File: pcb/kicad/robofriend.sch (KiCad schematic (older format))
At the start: 124 parts, among them J1 UART, J10 12V-Buck, J11 12V-Buck-Boost, J12 5VIN, J13 5VOUT, J14 5VOUT, J15 US2, J16 US3, J17 USB_A_4_PIN, J18 12V-Reg, J19 MON/AMP, J2 VBAT, J20 US4, J21 MRi, J22 SPI, J23 MRi, J24 3V3OUT, J25 3V3OUT, J26 M1, J27 M2, J28 IR1, J29 ADC1, J3 PWR, J30 IR2, J31 ADC2, J32 IR3, J33 GS2, J4 GS2, J5 I2C, J6 I2C, J7 I2C, J8 I2C, J9 US1, K1 Schrak-RT334012, Q1 NMOS, Q2 NPN, Q3 PMOS, U1 74LVC1T45, U10 TL331, U2 Teensy++2.0, U3 TL331, U4 74LVC1T45, U5 PCA9517, U6 MCP6001, U7 LM3940-3.3, U8 LM4040, U9 INA193

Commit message: added new usb connector footprint to layout, minor adaptations, generated gerber and drill files, new plot available
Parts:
- J17: footprint USB_A_4_PIN:MOLEX_48258_0001 -> USB_A_4_PIN:WURTH_61400416021
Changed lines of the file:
@@
 F 0 "J17" H 7425 2225 50  0000 L CNN
 F 1 "USB_A_4_PIN" H 7425 2125 50  0000 L CNN
-F 2 "USB_A_4_PIN:MOLEX_48258_0001" H 7775 1725 50  0001 C CNN
+F 2 "USB_A_4_PIN:WURTH_61400416021" H 7775 1725 50  0001 C CNN
 F 3 "" H 7775 1725 50  0001 C CNN
 F 4 "48258-0001" H 7625 1775 60  0001 C CNN "Part No"

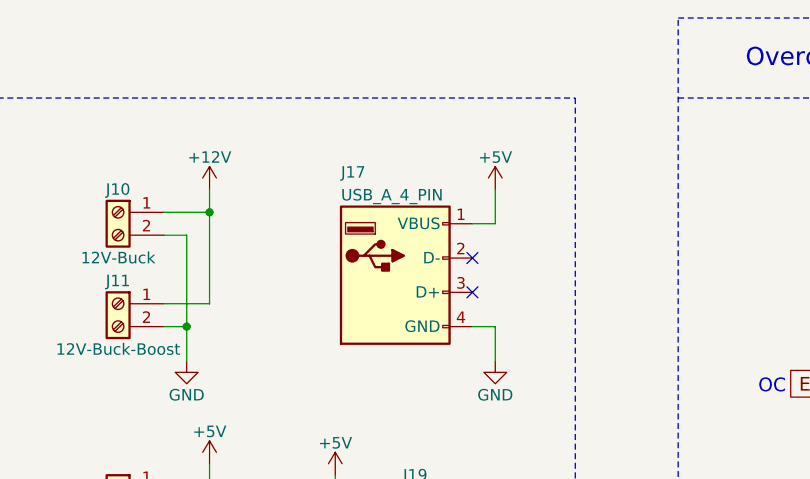
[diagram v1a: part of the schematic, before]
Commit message: adapting paths to work in linux
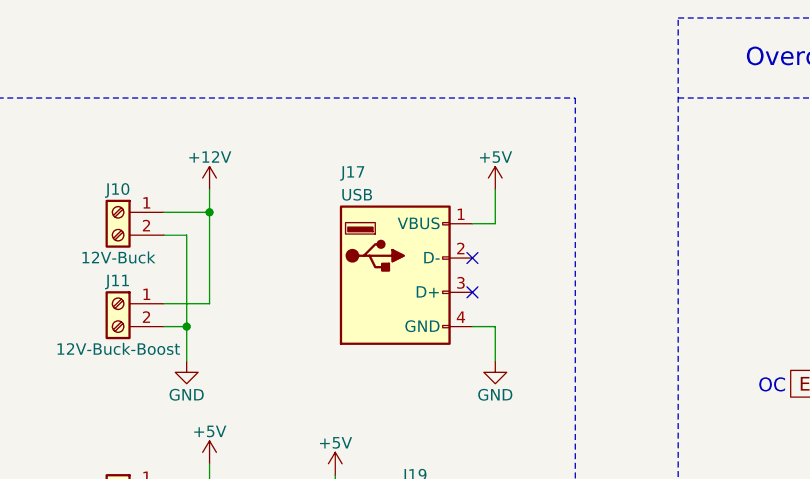
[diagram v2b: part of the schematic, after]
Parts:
- J17: value USB_A_4_PIN -> USB; footprint USB_A_4_PIN:WURTH_61400416021 -> USB:WURTH_61400416021
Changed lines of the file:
@@
 P 7625 1775
 F 0 "J17" H 7425 2225 50  0000 L CNN
-F 1 "USB_A_4_PIN" H 7425 2125 50  0000 L CNN
-F 2 "USB_A_4_PIN:WURTH_61400416021" H 7775 1725 50  0001 C CNN
+F 1 "USB" H 7425 2125 50  0000 L CNN
+F 2 "USB:WURTH_61400416021" H 7775 1725 50  0001 C CNN
 F 3 "" H 7775 1725 50  0001 C CNN
 F 4 "48258-0001" H 7625 1775 60  0001 C CNN "Part No"

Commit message: adpated paths in linux, rescued some libs, minor clean-up
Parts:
- JP2, JP3, JP5: symbol Jumper_NC_Dual -> Jumper_NC_Dual-RESCUE-robofriend
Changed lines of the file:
@@
 EESchema Schematic File Version 2
+LIBS:robofriend-rescue
 LIBS:power
 LIBS:device
@@
 $EndComp
 $Comp
-L Jumper_NC_Dual JP5
+L Jumper_NC_Dual-RESCUE-robofriend JP5
 U 1 1 5B086E62
 P 13850 8600
@@
 $Bitmap
 Pos 15500 10270
-Scale 1.000000
+Scale 1,000000
 Data
 89 50 4E 47 0D 0A 1A 0A 00 00 00 0D 49 48 44 52 00 00 01 2C 00 00 00 A0 08 06 00 00 00 B6 78 51
@@
 $EndComp
 $Comp
-L Jumper_NC_Dual JP3
+L Jumper_NC_Dual-RESCUE-robofriend JP3
 U 1 1 5B3C6796
 P 6450 8600
@@
 $EndComp
 $Comp
-L Jumper_NC_Dual JP2
+L Jumper_NC_Dual-RESCUE-robofriend JP2
 U 1 1 5B714FC0
 P 3150 4650

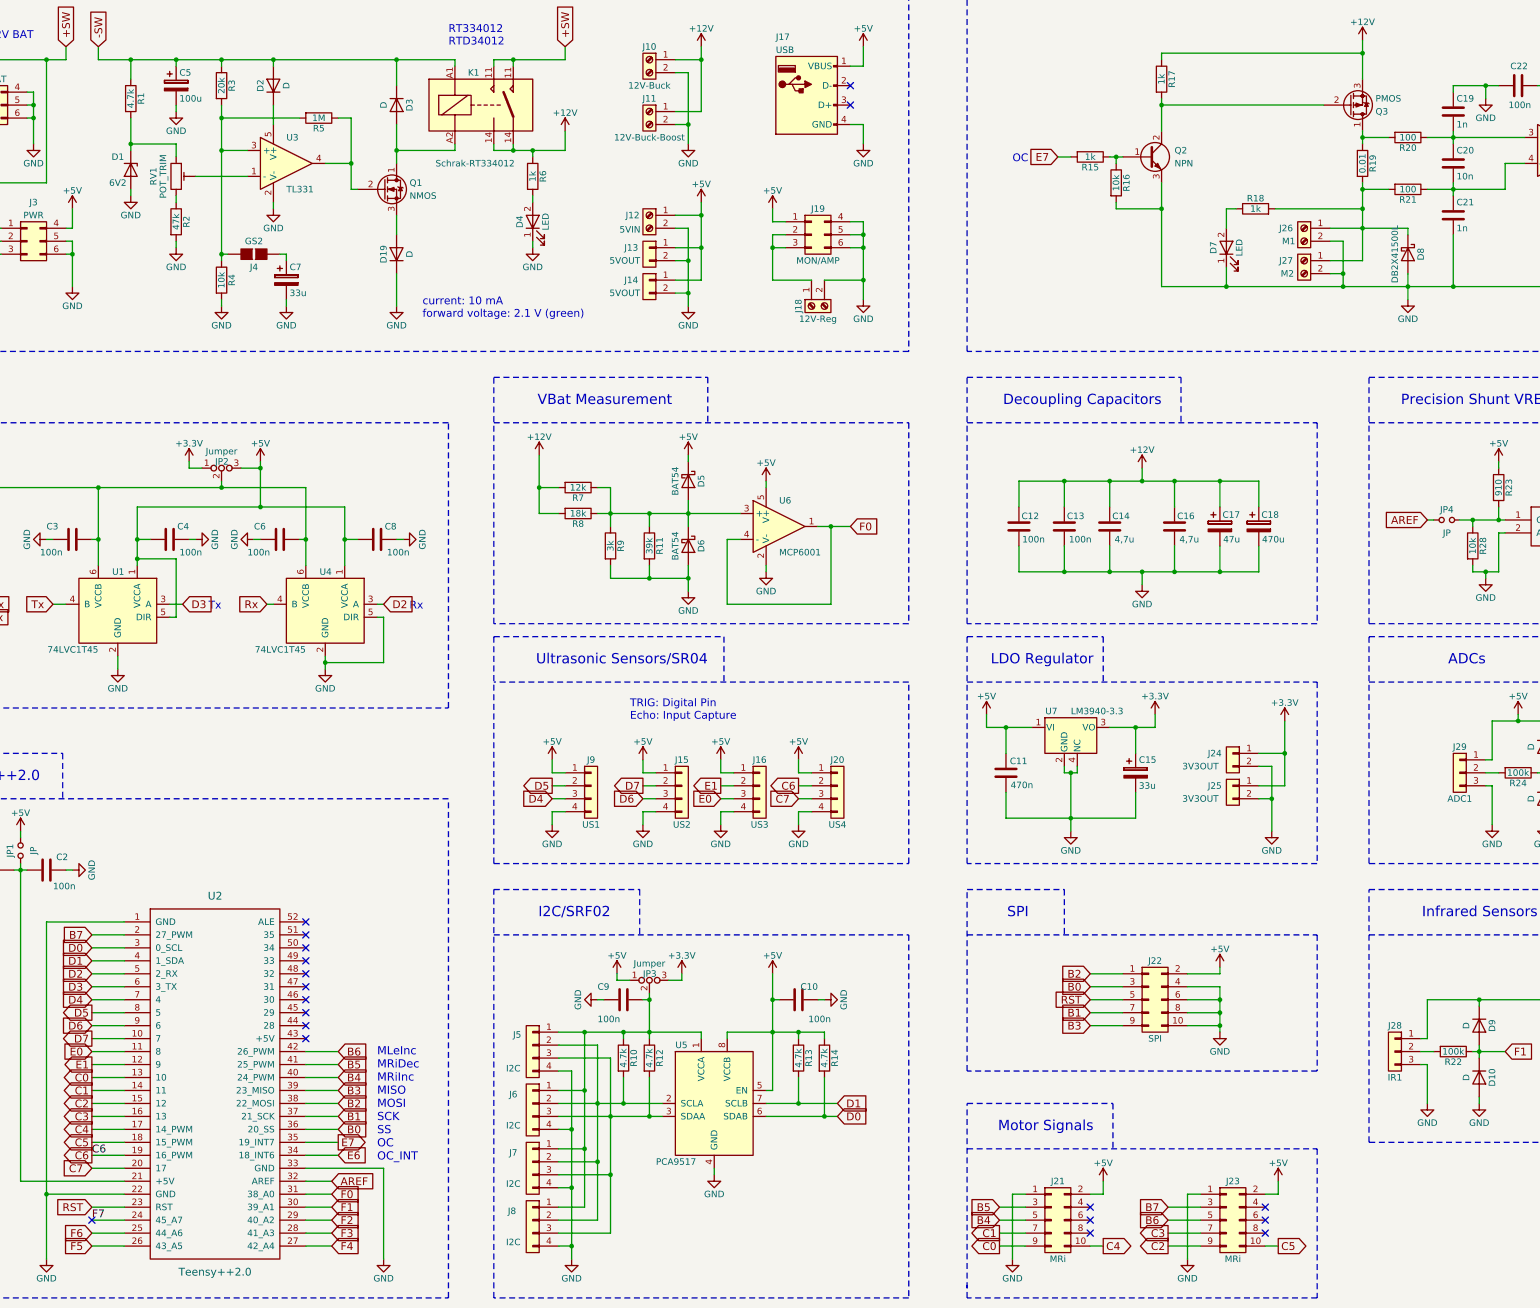
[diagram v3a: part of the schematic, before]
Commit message: corrected npn, nmos and pmos orientation
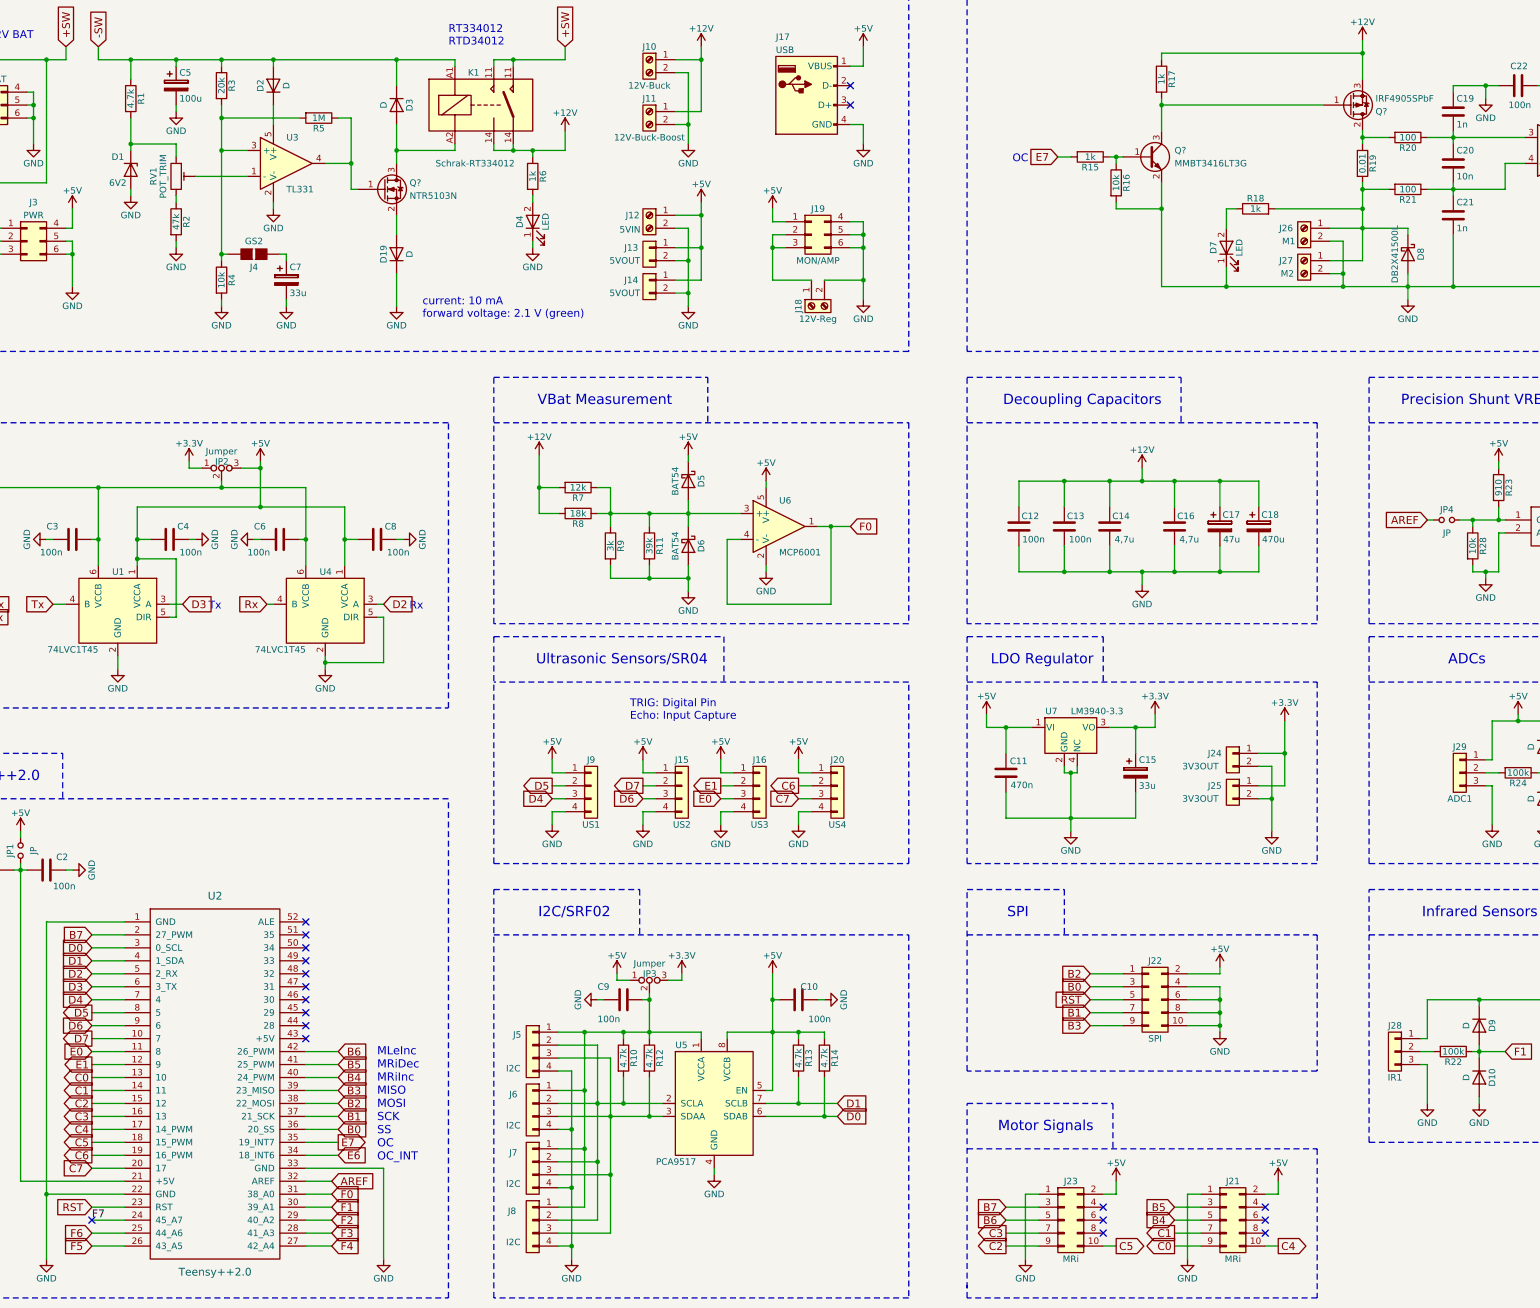
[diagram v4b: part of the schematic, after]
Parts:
- removed Q1: NMOS, TO_SOT_Packages_SMD:SOT-23, symbol Q_NMOS_DGS
- removed Q2: NPN, TO_SOT_Packages_SMD:SOT-23, symbol Q_NPN_BCE
- removed Q3: PMOS, TO_SOT_Packages_SMD:TO-263-2, symbol Q_PMOS_DGS
- added Q?: NTR5103N, TO_SOT_Packages_SMD:SOT-23, symbol Q_NMOS_GSD
- added Q?: MMBT3416LT3G, TO_SOT_Packages_SMD:SOT-23, symbol Q_NPN_BEC
- added Q?: IRF4905SPbF, TO_SOT_Packages_SMD:TO-263-2, symbol Q_PMOS_GDS
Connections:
- net +12V: now also Q?.3 (S)
- net GND: now also Q?.2 (E)
- net at D3.2 (A), K1.A2: now also Q?.3 (D)
- net at R5.1, U3.4: now also Q?.1 (G)
- net at D19.2 (A): now also Q?.2 (S)
- net at R19.1, R20.2: now also Q?.2 (D)
- net at R17.2: now also Q?.1 (G), Q?.3 (C)
- net at R15.1, R16.1: now also Q?.1 (B)
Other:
- moved on the sheet: J21, J23
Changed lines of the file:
@@
 Comment4 ""
 $EndDescr
-Text Label 2150 9950 0    60   ~ 0
-C6
 Text Label 2250 10450 2    60   ~ 0
 F7
@@
 NoConn ~ 3800 8850
 NoConn ~ 3800 8950
-NoConn ~ 11200 10350
-NoConn ~ 11200 10450
-NoConn ~ 11200 10550
+NoConn ~ 9950 10350
+NoConn ~ 9950 10450
+NoConn ~ 9950 10550
 $Comp
 L Conn_02x05_Odd_Even J22
@@
 $Bitmap
 Pos 15500 10270
-Scale 1,000000
+Scale 1.000000
 Data
 89 50 4E 47 0D 0A 1A 0A 00 00 00 0D 49 48 44 52 00 00 01 2C 00 00 00 A0 08 06 00 00 00 B6 78 51
@@
 NoConn ~ 13950 5100
 $Comp
-L Q_NMOS_DGS Q1
-U 1 1 5B2C98C6
-P 4400 2500
-F 0 "Q1" H 4600 2550 50  0000 L CNN
-F 1 "NMOS" H 4600 2450 50  0000 L CNN
-F 2 "TO_SOT_Packages_SMD:SOT-23" H 4600 2600 50  0001 C CNN
-F 3 "" H 4400 2500 50  0001 C CNN
-	1    4400 2500
-	1    0    0    -1
-$EndComp
-$Comp
 L D D3
 U 1 1 5B2C9F38
@@
 $EndComp
 $Comp
-L Q_PMOS_DGS Q3
-U 1 1 5B2D2545
-P 11850 1850
-F 0 "Q3" H 12050 1900 50  0000 L CNN
-F 1 "PMOS" H 12050 1800 50  0000 L CNN
-F 2 "TO_SOT_Packages_SMD:TO-263-2" H 12050 1950 50  0001 C CNN
-F 3 "" H 11850 1850 50  0001 C CNN
-F 4 "IRF4905STRLPBF" H 11850 1850 60  0001 C CNN "Part No"
-	1    11850 1850
-	1    0    0    1
-$EndComp
-$Comp
 L R R17
 U 1 1 5B2D2966
@@
 $EndComp
 $Comp
-L Q_NPN_BCE Q2
-U 1 1 5B2D2E70
-P 10300 2250
-F 0 "Q2" H 10500 2300 50  0000 L CNN
-F 1 "NPN" H 10500 2200 50  0000 L CNN
-F 2 "TO_SOT_Packages_SMD:SOT-23" H 10500 2350 50  0001 C CNN
-F 3 "" H 10300 2250 50  0001 C CNN
-	1    10300 2250
-	1    0    0    -1
-$EndComp
-$Comp
 L R R20
 U 1 1 5B2D44D6
@@
 L +5V #PWR038
 U 1 1 5B343A88
-P 11300 10150
-F 0 "#PWR038" H 11300 10000 50  0001 C CNN
-F 1 "+5V" H 11300 10290 50  0000 C CNN
-F 2 "" H 11300 10150 50  0001 C CNN
-F 3 "" H 11300 10150 50  0001 C CNN
-	1    11300 10150
+P 10050 10150
+F 0 "#PWR038" H 10050 10000 50  0001 C CNN
+F 1 "+5V" H 10050 10290 50  0000 C CNN
+F 2 "" H 10050 10150 50  0001 C CNN
+F 3 "" H 10050 10150 50  0001 C CNN
+	1    10050 10150
 	-1   0    0    -1
 $EndComp
@@
 L +5V #PWR039
 U 1 1 5B343F62
-P 9950 10150
-F 0 "#PWR039" H 9950 10000 50  0001 C CNN
-F 1 "+5V" H 9950 10290 50  0000 C CNN
-F 2 "" H 9950 10150 50  0001 C CNN
-F 3 "" H 9950 10150 50  0001 C CNN
-	1    9950 10150
+P 11300 10150
+F 0 "#PWR039" H 11300 10000 50  0001 C CNN
+F 1 "+5V" H 11300 10290 50  0000 C CNN
+F 2 "" H 11300 10150 50  0001 C CNN
+F 3 "" H 11300 10150 50  0001 C CNN
+	1    11300 10150
 	-1   0    0    -1
 $EndComp
-NoConn ~ 9850 10350
-NoConn ~ 9850 10450
-NoConn ~ 9850 10550
+NoConn ~ 11200 10350
+NoConn ~ 11200 10450
+NoConn ~ 11200 10550
 $Comp
 L GND #PWR040
 U 1 1 5B3458AE
-P 9250 10750
-F 0 "#PWR040" H 9250 10500 50  0001 C CNN
-F 1 "GND" H 9250 10600 50  0000 C CNN
-F 2 "" H 9250 10750 50  0001 C CNN
-F 3 "" H 9250 10750 50  0001 C CNN
-	1    9250 10750
-	1    0    0    -1
-$EndComp
-$Comp
-L GND #PWR041
-U 1 1 5B346524
 P 10600 10750
-F 0 "#PWR041" H 10600 10500 50  0001 C CNN
+F 0 "#PWR040" H 10600 10500 50  0001 C CNN
 F 1 "GND" H 10600 10600 50  0000 C CNN
 F 2 "" H 10600 10750 50  0001 C CNN
@@
 	1    0    0    -1
 $EndComp
-Text GLabel 9150 10550 0    60   Output ~ 0
+$Comp
+L GND #PWR041
+U 1 1 5B346524
+P 9350 10750
+F 0 "#PWR041" H 9350 10500 50  0001 C CNN
+F 1 "GND" H 9350 10600 50  0000 C CNN
+F 2 "" H 9350 10750 50  0001 C CNN
+F 3 "" H 9350 10750 50  0001 C CNN
+	1    9350 10750
+	1    0    0    -1
+$EndComp
+Text GLabel 10500 10550 0    60   Output ~ 0
 C1
-Text GLabel 9150 10650 0    60   Output ~ 0
+Text GLabel 10500 10650 0    60   Output ~ 0
 C0
-Text GLabel 9950 10650 2    60   Output ~ 0
-C4
 Text GLabel 11300 10650 2    60   Output ~ 0
+C4
+Text GLabel 10050 10650 2    60   Output ~ 0
 C5
-Text GLabel 10450 10550 0    60   Output ~ 0
+Text GLabel 9200 10550 0    60   Output ~ 0
 C3
-Text GLabel 10450 10650 0    60   Output ~ 0
+Text GLabel 9200 10650 0    60   Output ~ 0
 C2
 $Comp
@@
 Text Notes 4350 10000 0    63   ~ 0
 MLeInc\nMRiDec\nMRiInc\nMISO\nMOSI\nSCK\nSS\nOC\nOC_INT
-Text GLabel 9150 10350 0    60   Input ~ 0
+Text GLabel 10500 10350 0    60   Input ~ 0
 B5
-Text GLabel 9150 10450 0    60   Input ~ 0
+Text GLabel 10500 10450 0    60   Input ~ 0
 B4
-Text GLabel 10450 10450 0    60   Input ~ 0
+Text GLabel 9200 10450 0    60   Input ~ 0
 B6
-Text GLabel 10450 10350 0    60   Input ~ 0
+Text GLabel 9200 10350 0    60   Input ~ 0
 B7
 Text Notes 1050 9290 0    62   ~ 0
@@
 	1450 2800 1300 2800
 Wire Wire Line
-	11200 10650 11300 10650
+	9950 10650 10050 10650
 Wire Wire Line
-	10700 10650 10450 10650
+	9450 10650 9200 10650
 Wire Wire Line
-	10700 10550 10450 10550
+	9450 10550 9200 10550
 Wire Wire Line
-	10700 10450 10450 10450
+	9450 10450 9200 10450
 Wire Wire Line
-	10700 10350 10450 10350
+	9450 10350 9200 10350
 Wire Wire Line
-	11300 10250 11200 10250
+	10050 10250 9950 10250
 Wire Wire Line
-	11300 10150 11300 10250
+	10050 10150 10050 10250
 Wire Wire Line
-	10600 10250 10600 10750
+	9350 10250 9350 10750
 Wire Wire Line
-	10700 10250 10600 10250
+	9450 10250 9350 10250
 Wire Wire Line
-	9350 10650 9150 10650
+	10700 10650 10500 10650
 Wire Wire Line
-	9350 10550 9150 10550
+	10700 10550 10500 10550
 Wire Wire Line
-	9350 10450 9150 10450
+	10700 10450 10500 10450
 Wire Wire Line
-	9350 10350 9150 10350
+	10700 10350 10500 10350
 Wire Wire Line
-	9250 10250 9250 10750
+	10600 10250 10600 10750
 Wire Wire Line
-	9350 10250 9250 10250
+	10700 10250 10600 10250
 Wire Wire Line
-	9850 10650 9950 10650
+	11200 10650 11300 10650
 Wire Wire Line
-	9950 10250 9950 10150
+	11300 10250 11300 10150
 Wire Wire Line
-	9850 10250 9950 10250
+	11200 10250 11300 10250
 Wire Wire Line
 	2400 10350 2150 10350
@@
 L Conn_02x05_Odd_Even J21
 U 1 1 5B720475
-P 9550 10450
-F 0 "J21" H 9600 10750 50  0000 C CNN
-F 1 "MRi" H 9600 10150 50  0000 C CNN
-F 2 "Pin_Headers:Pin_Header_Straight_2x05_Pitch2.54mm" H 9550 10450 50  0001 C CNN
-F 3 "" H 9550 10450 50  0001 C CNN
-	1    9550 10450
-	1    0    0    -1
-$EndComp
-$Comp
-L Conn_02x05_Odd_Even J23
-U 1 1 5B7225DB
 P 10900 10450
-F 0 "J23" H 10950 10750 50  0000 C CNN
+F 0 "J21" H 10950 10750 50  0000 C CNN
 F 1 "MRi" H 10950 10150 50  0000 C CNN
 F 2 "Pin_Headers:Pin_Header_Straight_2x05_Pitch2.54mm" H 10900 10450 50  0001 C CNN
@@
 $EndComp
 $Comp
+L Conn_02x05_Odd_Even J23
+U 1 1 5B7225DB
+P 9650 10450
+F 0 "J23" H 9700 10750 50  0000 C CNN
+F 1 "MRi" H 9700 10150 50  0000 C CNN
+F 2 "Pin_Headers:Pin_Header_Straight_2x05_Pitch2.54mm" H 9650 10450 50  0001 C CNN
+F 3 "" H 9650 10450 50  0001 C CNN
+	1    9650 10450
+	1    0    0    -1
+$EndComp
+$Comp
 L Schrak-RT334012WG K1
 U 1 1 5B7C9BC5
@@
 	9750 7000 9750 6950
 Connection ~ 9700 7000
+$Comp
+L Q_NMOS_GSD Q?
+U 1 1 5BA4A30E
+P 4400 2500
+F 0 "Q?" H 4600 2550 50  0000 L CNN
+F 1 "NTR5103N" H 4600 2450 50  0000 L CNN
+F 2 "TO_SOT_Packages_SMD:SOT-23" H 4600 2600 50  0001 C CNN
+F 3 "" H 4400 2500 50  0001 C CNN
+	1    4400 2500
+	1    0    0    -1
+$EndComp
+$Comp
+L Q_NPN_BEC Q?
+U 1 1 5BA4E20D
+P 10300 2250
+F 0 "Q?" H 10500 2300 50  0000 L CNN
+F 1 "MMBT3416LT3G" H 10500 2200 50  0000 L CNN
+F 2 "TO_SOT_Packages_SMD:SOT-23" H 10500 2350 50  0001 C CNN
+F 3 "" H 10300 2250 50  0001 C CNN
+	1    10300 2250
+	1    0    0    -1
+$EndComp
+$Comp
+L Q_PMOS_GDS Q?
+U 1 1 5BA4FF36
+P 11850 1850
+F 0 "Q?" H 12050 1900 50  0000 L CNN
+F 1 "IRF4905SPbF" H 12050 1800 50  0000 L CNN
+F 2 "TO_SOT_Packages_SMD:TO-263-2" H 12050 1950 50  0001 C CNN
+F 3 "" H 11850 1850 50  0001 C CNN
+	1    11850 1850
+	1    0    0    1
+$EndComp
 $EndSCHEMATC

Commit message: minor changes on schematics
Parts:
- gave numbers to parts that had none: 3
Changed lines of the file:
@@
 Connection ~ 9700 7000
 $Comp
-L Q_NMOS_GSD Q?
+L Q_NMOS_GSD Q1
 U 1 1 5BA4A30E
 P 4400 2500
-F 0 "Q?" H 4600 2550 50  0000 L CNN
+F 0 "Q1" H 4600 2550 50  0000 L CNN
 F 1 "NTR5103N" H 4600 2450 50  0000 L CNN
 F 2 "TO_SOT_Packages_SMD:SOT-23" H 4600 2600 50  0001 C CNN
@@
 $EndComp
 $Comp
-L Q_NPN_BEC Q?
+L Q_NPN_BEC Q2
 U 1 1 5BA4E20D
 P 10300 2250
-F 0 "Q?" H 10500 2300 50  0000 L CNN
+F 0 "Q2" H 10500 2300 50  0000 L CNN
 F 1 "MMBT3416LT3G" H 10500 2200 50  0000 L CNN
 F 2 "TO_SOT_Packages_SMD:SOT-23" H 10500 2350 50  0001 C CNN
@@
 $EndComp
 $Comp
-L Q_PMOS_GDS Q?
+L Q_PMOS_GDS Q3
 U 1 1 5BA4FF36
 P 11850 1850
-F 0 "Q?" H 12050 1900 50  0000 L CNN
+F 0 "Q3" H 12050 1900 50  0000 L CNN
 F 1 "IRF4905SPbF" H 12050 1800 50  0000 L CNN
 F 2 "TO_SOT_Packages_SMD:TO-263-2" H 12050 1950 50  0001 C CNN

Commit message: added a solder jumper to connect the buck-boost-out and buck-boost-in
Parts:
- added J?: GS2, Connectors:GS2, symbol GS2
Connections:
- net +12V: now also J?.2 (G2)
- net at J18.1 (Pin_1), J19.2 (Pin_2), J19.3 (Pin_3): now also J?.1 (G1)
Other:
- moved on the sheet: J17, J18, J19

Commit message: working on hardware rev ii > corrected transistor and fet pin assignments, corrected motor signal pinheaders, routed, ...
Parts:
- J22: renamed from J23; value MRi -> MLe
- gave numbers to parts that had none: 1
- renumbered D9 to D10, D10 to D11, D11 to D12, D12 to D13, D13 to D14, D14 to D15, D15 to D16, D16 to D17, D17 to D18, D18 to D19, D19 to D4, D4 to D5, D5 to D6, D6 to D7, D7 to D8, D8 to D9, J16 to J17, J17 to J18, J18 to J20, J20 to J21, J22 to J23, J21 to J24, J24 to J25, J25 to J26, J26 to J27, J27 to J28, J28 to J29, J29 to J30, J30 to J31, J31 to J32, J32 to J33, J33 to J34, R28 to R23, R23 to R24, R24 to R25, R25 to R26, R26 to R27, R27 to R28, U9 to U8, U8 to U9
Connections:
- net +5V: now also J22.1 (Pin_1), J24.1 (Pin_1); no longer J22.2 (Pin_2), J24.2 (Pin_2)
- net B4: now also J24.6 (Pin_6); no longer J24.5 (Pin_5)
- net B5: now also J24.4 (Pin_4); no longer J24.3 (Pin_3)
- net B6: now also J22.6 (Pin_6); no longer J22.5 (Pin_5)
- net B7: now also J22.4 (Pin_4); no longer J22.3 (Pin_3)
- net C0: now also J24.8 (Pin_8); no longer J24.9 (Pin_9)
- net C1: now also J24.10 (Pin_10); no longer J24.7 (Pin_7)
- net C2: now also J22.10 (Pin_10); no longer J22.9 (Pin_9)
- net C3: now also J22.8 (Pin_8); no longer J22.7 (Pin_7)
- net C4: now also J24.9 (Pin_9); no longer J24.10 (Pin_10)
- net C5: now also J22.9 (Pin_9); no longer J22.10 (Pin_10)
- net GND: now also J22.2 (Pin_2), J24.2 (Pin_2); no longer J22.1 (Pin_1), J24.1 (Pin_1)

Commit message: adapted u10, pull-up on schematic
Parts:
- added R?: 5.1k, Resistors_SMD:R_0805, symbol R
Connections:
- net +5V: now also R?.2
- net E6: now also R?.1
- net at RV2.2: now also U10.3 (+); no longer U10.1 (-)
- net at J34.2 (G2), U8.1: now also U10.1 (-); no longer U10.3 (+)
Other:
- note added: "MLeInc\nMRiDec\nMRiInc\nMISO\nMOSI\nSCK\nSS\nOC\n~OC_INT"
- note added: "~OC_INT"
- note removed: "MLeInc\nMRiDec\nMRiInc\nMISO\nMOSI\nSCK\nSS\nOC\nOC_INT"
- note removed: "OC_INT"
- moved on the sheet: C23, J34, RV2
